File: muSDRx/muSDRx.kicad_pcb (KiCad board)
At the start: 2 copper layers, 100 x 100 mm, 124 parts, among them J1 Conn_01x02_Male, J11 Conn_01x02_Male, J2 Conn_01x02_Male, J3 Conn_01x02_Male, J4 Conn_01x02_Male, J5 Conn_01x02_Male, J6 Conn_01x02_Male, J7 35RAPC4BHN2, J8 35RAPC4BHN2, J9 Conn_01x04_Male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

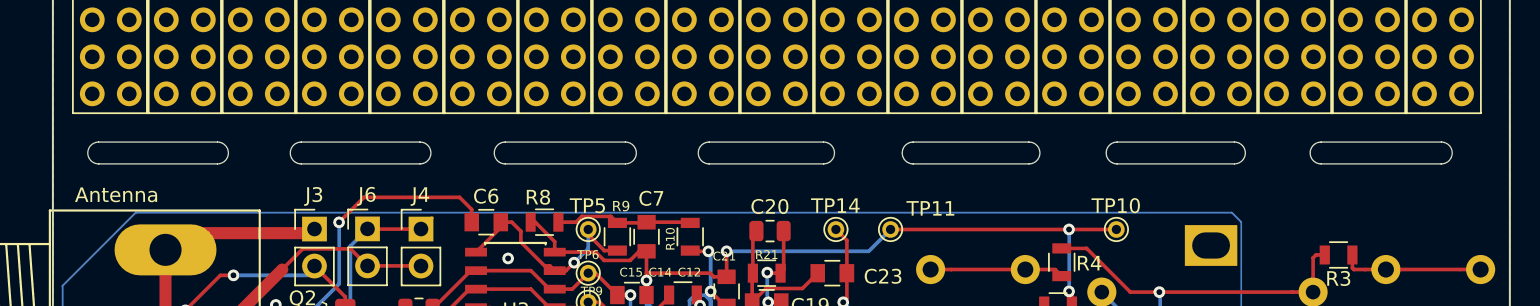
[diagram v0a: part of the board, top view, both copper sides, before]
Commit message: Changed the feedback resistors and caps for the I&Q channels to tweaked values.
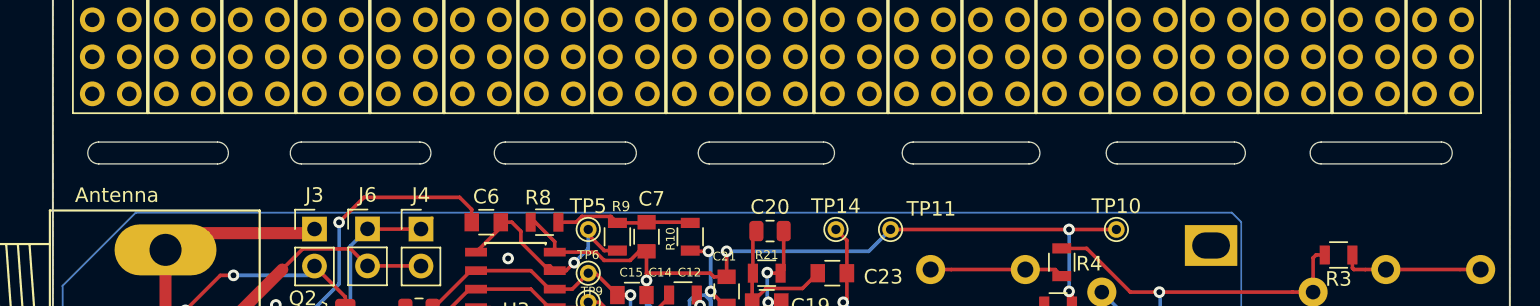
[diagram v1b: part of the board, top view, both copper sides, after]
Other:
- net class Default removed
